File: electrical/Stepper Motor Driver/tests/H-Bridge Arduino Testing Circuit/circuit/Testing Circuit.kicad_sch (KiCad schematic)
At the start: 26 parts, among them M1 Stepper_Motor_bipolar, Q1 NMOS, Q2 NMOS, Q3 NMOS, Q4 NMOS, Q5 NMOS, Q6 NMOS, Q7 NMOS, Q8 NMOS, U1 UCC27710D, U2 UCC27710D, U3 UCC27710D, U4 UCC27710D

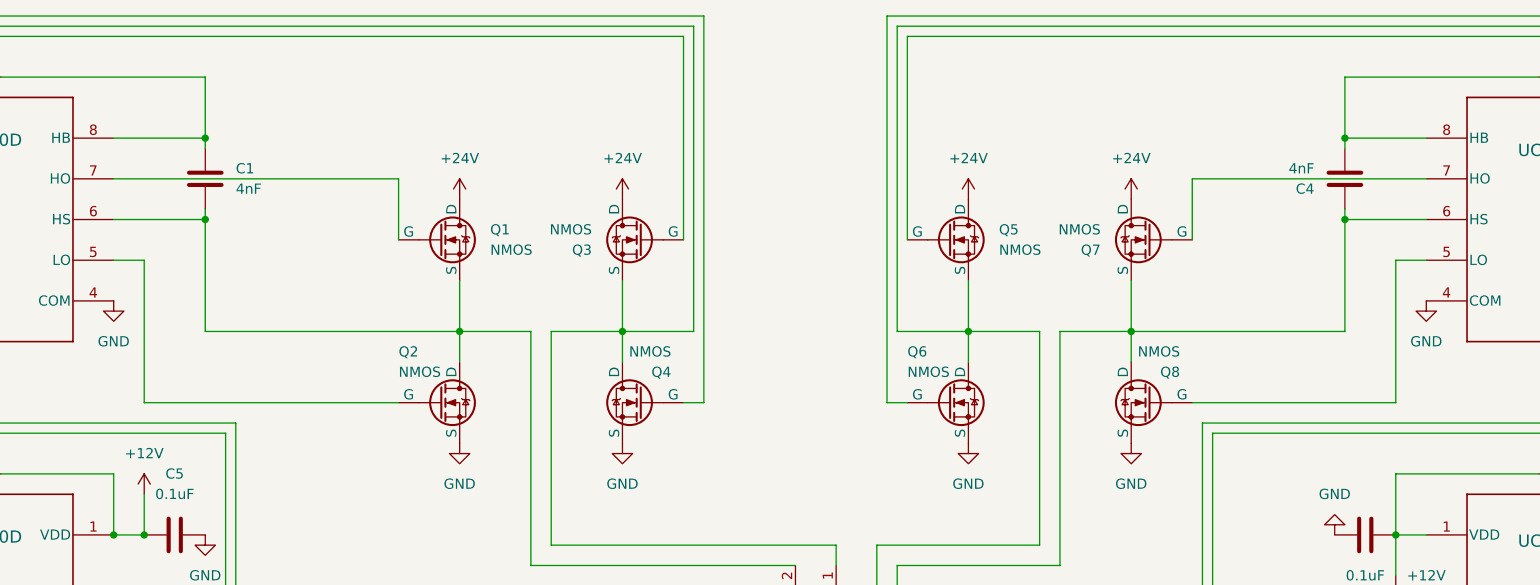
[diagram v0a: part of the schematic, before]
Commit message: Adding correct nMOS symbol
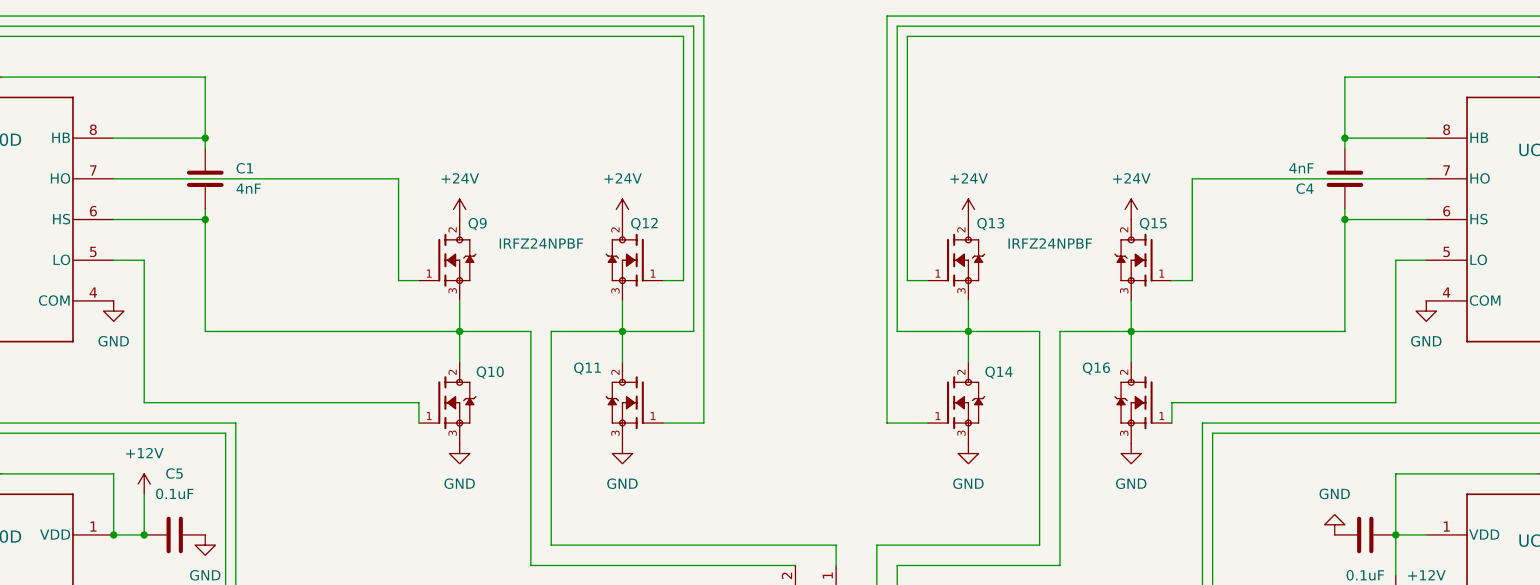
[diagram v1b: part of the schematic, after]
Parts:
- removed Q1, Q2, Q3, Q4, Q5, Q6, Q7, Q8: NMOS, symbol Simulation_SPICE:NMOS
- added Q10, Q11, Q12, Q13, Q14, Q15, Q16, Q9: IRFZ24NPBF, IRFZ24NPBF:TO254P1041X444X1930-3P, symbol IRFZ24NPBF:IRFZ24NPBF
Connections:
- net +24V: now also Q12.2, Q13.2, Q15.2, Q9.2
- net GND: now also Q10.3, Q11.3, Q14.3, Q16.3
- net at U1.5 (LO): now also Q10.1
- net at C1.2, M1.2 (-), U1.6 (HS): now also Q10.2, Q9.3
- net at U1.7 (HO): now also Q9.1
- net at U4.5 (LO): now also Q14.1
- net at C3.2, M1.3, U4.6 (HS): now also Q13.3, Q14.2
- net at U4.7 (HO): now also Q13.1
- net at U2.7 (HO): now also Q12.1
- net at C2.1, M1.1, U2.6 (HS): now also Q11.2, Q12.3
- net at U2.5 (LO): now also Q11.1
- net at U3.5 (LO): now also Q16.1
- net at C4.1, M1.4, U3.6 (HS): now also Q15.3, Q16.2
- net at U3.7 (HO): now also Q15.1

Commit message: Final MOSFET selection and spice models
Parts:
- removed Q10, Q11, Q12, Q13, Q14, Q15, Q16, Q9: IRFZ24NPBF, IRFZ24NPBF:TO254P1041X444X1930-3P, symbol IRFZ24NPBF:IRFZ24NPBF
- added Q1, Q2, Q3, Q4, Q5, Q6, Q7, Q8: IRF530NPBF, IRF530NPBF:TO254P1041X444X1930-3, symbol IRF530NPBF:IRF530NPBF
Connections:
- net +24V: now also Q1.2, Q4.2, Q5.2, Q7.2
- net GND: now also Q2.3, Q3.3, Q6.3, Q8.3
- net at U1.5 (LO): now also Q2.1
- net at C1.2, M1.2 (-), U1.6 (HS): now also Q1.3, Q2.2
- net at U1.7 (HO): now also Q1.1
- net at U4.5 (LO): now also Q6.1
- net at C3.2, M1.3, U4.6 (HS): now also Q5.3, Q6.2
- net at U4.7 (HO): now also Q5.1
- net at U3.5 (LO): now also Q8.1
- net at C4.1, M1.4, U3.6 (HS): now also Q7.3, Q8.2
- net at U2.7 (HO): now also Q4.1
- net at C2.1, M1.1, U2.6 (HS): now also Q3.2, Q4.3
- net at U3.7 (HO): now also Q7.1
- net at U2.5 (LO): now also Q3.1

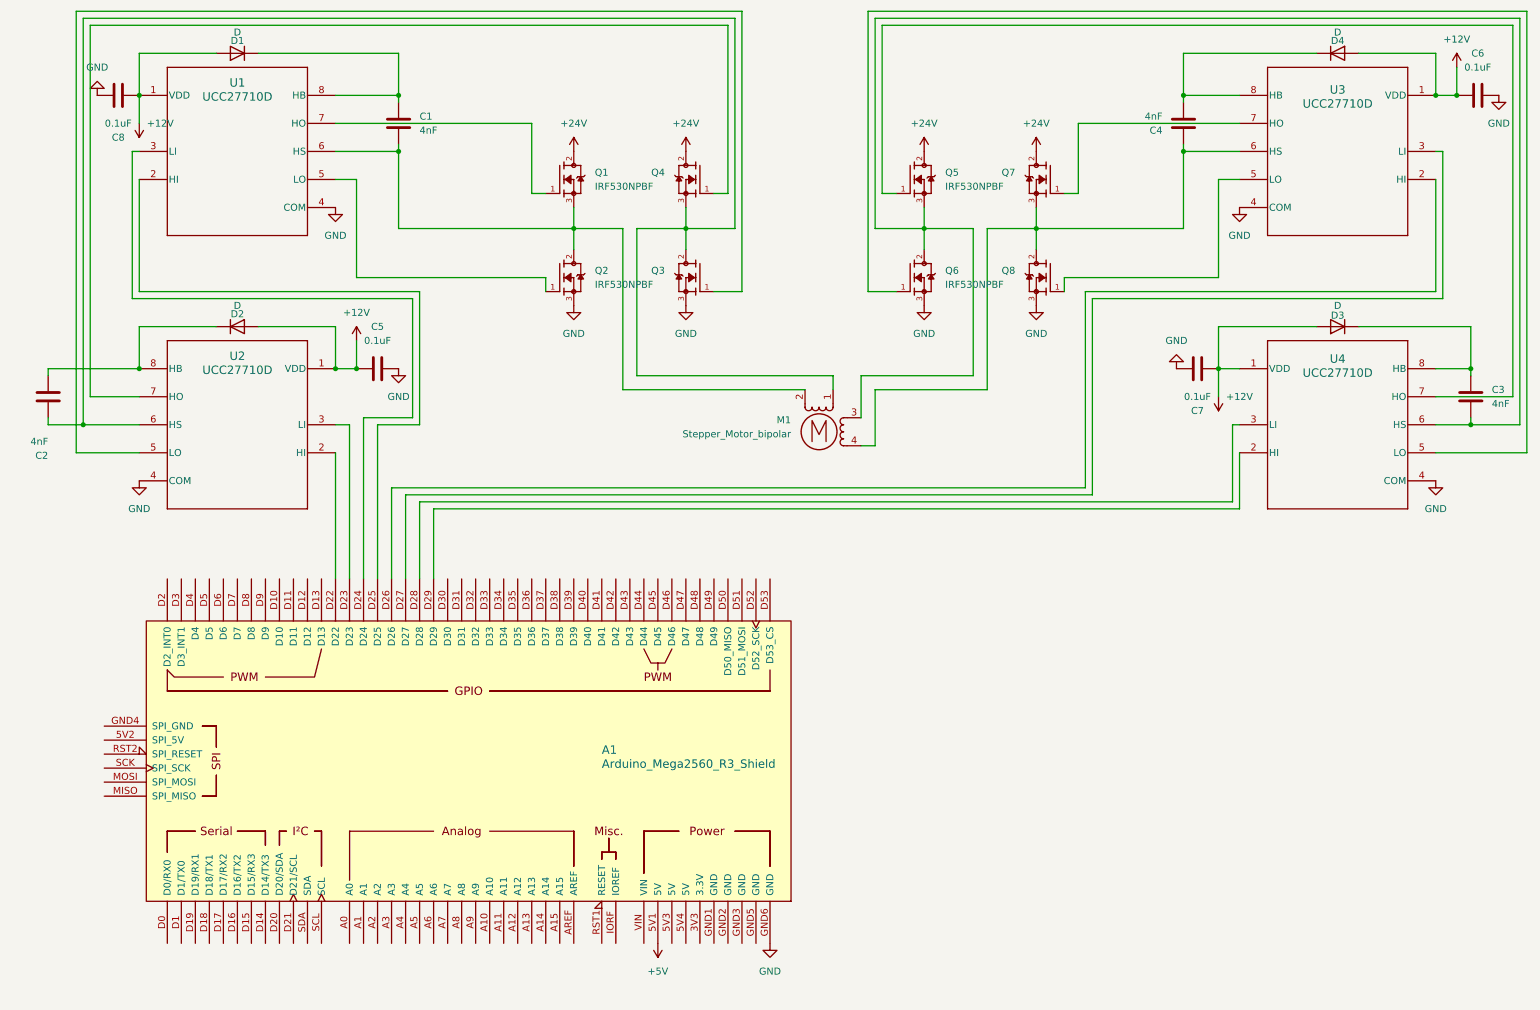
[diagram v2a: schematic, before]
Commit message: Adding motor spice model
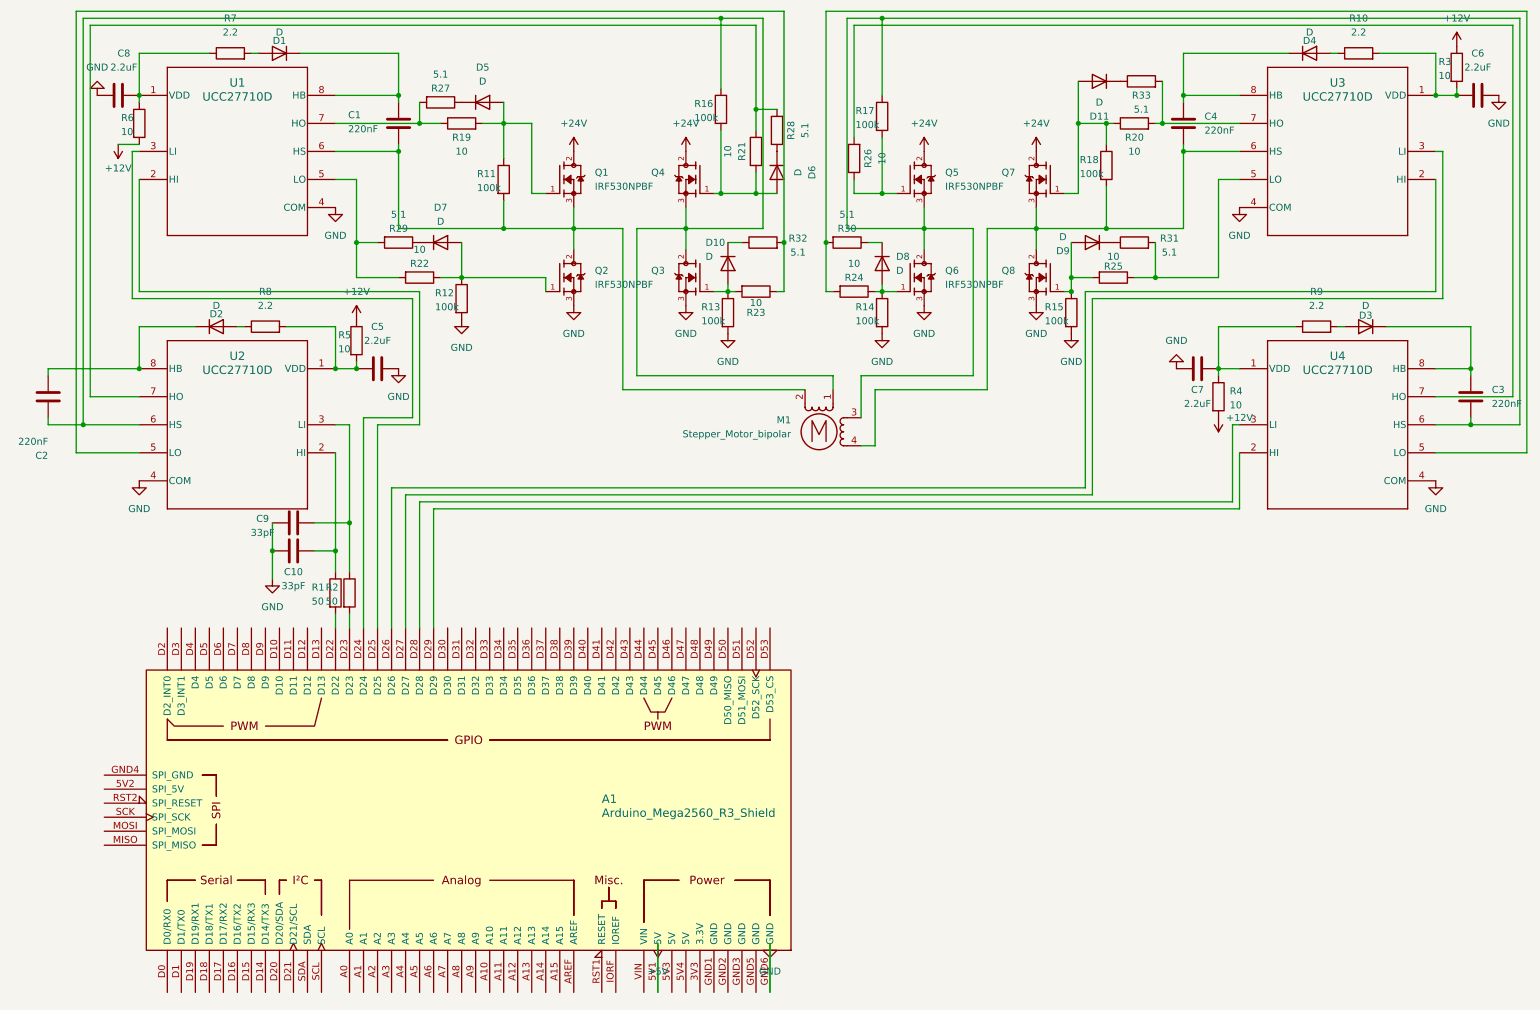
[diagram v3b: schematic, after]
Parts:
- added C10, C9: 33pF, symbol Device:C
- added D10, D11, D5, D6, D7, D8, D9: D, symbol Device:D
- added R1, R2: 50, symbol Device:R
- added R10, R7, R8, R9: 2.2, symbol Device:R
- added R11, R12, R13, R14, R15, R16, R17, R18: 100k, symbol Device:R
- added R19, R20, R21, R22, R23, R24, R25, R26, R3, R4, R5, R6: 10, symbol Device:R
- added R27, R28, R29, R30, R31, R32, R33: 5.1, symbol Device:R
- C1, C2, C3, C4: value 4nF -> 220nF
- C5, C6, C7, C8: value 0.1uF -> 2.2uF
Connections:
- net +12V: now also R3.1, R4.2, R5.1, R6.2; no longer C5.1, C6.1, C7.1, C8.1, D1.2 (A), D2.2 (A), D3.2 (A), D4.2 (A), U1.1 (VDD), U2.1 (VDD), U3.1 (VDD), U4.1 (VDD)
- net GND: now also C10.1, C9.1, R12.2, R13.2, R14.2, R15.2
- net at U1.5 (LO): now also R22.2, R29.2; no longer Q2.1
- net at C1.2, M1.2 (-), Q1.3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: now also R11.2
- net at U1.7 (HO): now also R19.1, R27.2; no longer Q1.1
- net at Q6.1: now also D8.2 (A), R14.1, R24.1; no longer U4.5 (LO)
- net at C3.2, M1.3, Q5.3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: now also R17.1
- net at Q5.1: now also R17.2, R26.1; no longer U4.7 (HO)
- net at U2.2 (HI): now also C10.2, R1.1; no longer A1.D22
- net at U2.3 (LI): now also C9.2, R2.1; no longer A1.D23
- net at U2.5 (LO): now also R23.1, R32.2; no longer Q3.1
- net at C2.1, M1.1, Q3.2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: now also R16.1
- net at U2.7 (HO): now also R21.1, R28.2; no longer Q4.1
- net at U3.5 (LO): now also R25.1, R31.2; no longer Q8.1
- net at C4.1, M1.4, Q7.3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: now also R18.2
- net at U3.7 (HO): now also R20.2, R33.2; no longer Q7.1
- new net: C8.1, R6.1, R7.1, U1.1 (VDD)
- new net: D10.2 (A), Q3.1, R13.1, R23.2
- new net: C7.1, R4.1, R9.1, U4.1 (VDD)
- new net: D6.1 (K), R28.1
- new net: D9.2 (A), Q8.1, R15.1, R25.2
- new net: D2.2 (A), R8.1
- new net: D6.2 (A), Q4.1, R16.2, R21.2
- new net: C5.1, R5.2, R8.2, U2.1 (VDD)
- new net: D4.2 (A), R10.1
- new net: C6.1, R10.2, R3.2, U3.1 (VDD)
- new net: D7.1 (K), R29.1
- new net: D7.2 (A), Q2.1, R12.1, R22.1
- new net: D9.1 (K), R31.1
- new net: D5.1 (K), R27.1
- new net: D1.2 (A), R7.2
- new net: R26.2, U4.7 (HO)
- new net: A1.D23, R2.2
- new net: D10.1 (K), R32.1
- new net: D11.1 (K), R33.1
- new net: D11.2 (A), Q7.1, R18.1, R20.1
- new net: D8.1 (K), R30.1
- new net: D5.2 (A), Q1.1, R11.1, R19.2
- new net: R24.2, R30.2, U4.5 (LO)
- new net: A1.D22, R1.2
- new net: D3.2 (A), R9.2
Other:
- moved on the sheet: A1, D1, D2, D3, D4

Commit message: Selecting diodes and adding all recommended components
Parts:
- removed D1, D10, D11, D2, D3, D4, D5, D6, D7, D8, D9: D, symbol Device:D
- added D1, D2, D3, D4: 1N5819, Diode_THT:D_DO-41_SOD81_P10.16mm_Horizontal, symbol Diode:1N5819
- added D13, D14, D15, D16, D17, D18, D19, D20: BAT43, Diode_THT:D_DO-35_SOD27_P7.62mm_Horizontal, symbol Diode:BAT43
- added R34: 5.1, symbol Device:R
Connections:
- net at C1.1, U1.8 (HB): now also D1.1 (K)
- net at Q3.1, R13.1, R23.2: now also D16.2 (A)
- net at R28.1: now also D15.1 (K)
- net at Q8.1, R15.1, R25.2: now also D18.2 (A)
- net at C2.2, U2.8 (HB): now also D2.1 (K)
- net at R8.1: now also D2.2 (A)
- net at Q4.1, R16.2, R21.2: now also D15.2 (A)
- net at Q6.1, R14.1, R24.1: now also D17.2 (A)
- net at Q5.1, R17.2, R26.1: now also D20.2 (A)
- net at R10.1: now also D4.2 (A)
- net at R29.1: now also D13.1 (K)
- net at Q2.1, R12.1, R22.1: now also D13.2 (A)
- net at R31.1: now also D18.1 (K)
- net at C4.2, U3.8 (HB): now also D4.1 (K)
- net at R27.1: now also D14.1 (K)
- net at R7.2: now also D1.2 (A)
- net at R26.2, U4.7 (HO): now also R34.2
- net at R32.1: now also D16.1 (K)
- net at R33.1: now also D19.1 (K)
- net at Q7.1, R18.1, R20.1: now also D19.2 (A)
- net at R30.1: now also D17.1 (K)
- net at Q1.1, R11.1, R19.2: now also D14.2 (A)
- net at C3.1, U4.8 (HB): now also D3.1 (K)
- net at R9.2: now also D3.2 (A)
- new net: D20.1 (K), R34.1

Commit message: Docs for H-Bridge + driver
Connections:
- net GND: no longer A1.GND6 (GND)
- net at C9.2, R2.1, U2.3 (LI): now also A1.D23
- net at R2.2: no longer A1.D23
- net at C10.2, R1.1, U2.2 (HI): now also A1.D22
- net at R1.2: no longer A1.D22
- net +5V: no longer names the net of A1.5V1 (5V)
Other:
- moved on the sheet: A1
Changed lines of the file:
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@@
 	)
 	(junction
+		(at 69.85 120.65)
+		(diameter 0)
+		(color 0 0 0 0)
+	)
+	(junction
 		(at 82.55 39.37)
 		(diameter 0)
@@
 	)
 	(junction
+		(at 67.31 120.65)
+		(diameter 0)
+		(color 0 0 0 0)
+	)
+	(junction
 		(at 67.31 116.84)
 		(diameter 0)
@@
 	(wire
 		(pts
-			(xy 125.73 196.85) (xy 125.73 187.96)
-		)
-		(stroke
-			(width 0)
-			(type default)
-		)
-	)
-	(wire
-		(pts
 			(xy 137.16 52.07) (xy 135.89 52.07)
 		)
@@
 	(wire
 		(pts
-			(xy 77.47 130.81) (xy 77.47 105.41)
+			(xy 77.47 132.08) (xy 77.47 105.41)
 		)
 		(stroke
@@
 	(wire
 		(pts
-			(xy 80.01 130.81) (xy 80.01 106.68)
+			(xy 80.01 132.08) (xy 80.01 106.68)
 		)
 		(stroke
@@
 	(wire
 		(pts
-			(xy 67.31 128.27) (xy 67.31 130.81)
+			(xy 67.31 120.65) (xy 67.31 132.08)
 		)
 		(stroke
@@
 	(wire
 		(pts
-			(xy 69.85 128.27) (xy 69.85 130.81)
-		)
-		(stroke
-			(width 0)
-			(type default)
-		)
-	)
-	(wire
-		(pts
 			(xy 80.01 106.68) (xy 204.47 106.68)
 		)
@@
 	(wire
 		(pts
-			(xy 74.93 93.98) (xy 74.93 130.81)
+			(xy 74.93 93.98) (xy 74.93 132.08)
 		)
 		(stroke
@@
 	(wire
 		(pts
-			(xy 146.05 196.85) (xy 146.05 187.96)
-		)
-		(stroke
-			(width 0)
-			(type default)
-		)
-	)
-	(wire
-		(pts
 			(xy 207.01 58.42) (xy 194.31 58.42)
 		)
@@
 	(wire
 		(pts
+			(xy 69.85 120.65) (xy 69.85 132.08)
+		)
+		(stroke
+			(width 0)
+			(type default)
+		)
+	)
+	(wire
+		(pts
 			(xy 71.12 67.31) (xy 78.74 67.31)
 		)
@@
 	(wire
 		(pts
-			(xy 85.09 130.81) (xy 85.09 109.22)
+			(xy 85.09 132.08) (xy 85.09 109.22)
 		)
 		(stroke
@@
 	(wire
 		(pts
-			(xy 72.39 130.81) (xy 72.39 92.71)
+			(xy 72.39 132.08) (xy 72.39 92.71)
 		)
 		(stroke
@@
 	(wire
 		(pts
-			(xy 82.55 130.81) (xy 82.55 107.95)
+			(xy 82.55 132.08) (xy 82.55 107.95)
 		)
 		(stroke
@@
 	)
 	(symbol
-		(lib_id "power:+5V")
-		(at 125.73 187.96 180)
-		(unit 1)
-		(body_style 1)
-		(exclude_from_sim no)
-		(in_bom yes)
-		(on_board yes)
-		(in_pos_files yes)
-		(dnp no)
-		(fields_autoplaced yes)
-		(property "Reference" "#PWR021"
-			(at 125.73 184.15 0)
-			(hide yes)
-			(show_name no)
-			(do_not_autoplace no)
-			(effects
-				(font
-					(size 1.27 1.27)
-				)
-			)
-		)
-		(property "Value" "+5V"
-			(at 125.73 193.04 0)
-			(show_name no)
-			(do_not_autoplace no)
-			(effects
-				(font
-					(size 1.27 1.27)
-				)
-			)
-		)
-		(property "Footprint" ""
-			(at 125.73 187.96 0)
-			(hide yes)
-			(show_name no)
-			(do_not_autoplace no)
-			(effects
-				(font
-					(size 1.27 1.27)
-				)
-			)
-		)
-		(property "Datasheet" ""
-			(at 125.73 187.96 0)
-			(hide yes)
-			(show_name no)
-			(do_not_autoplace no)
-			(effects
-				(font
-					(size 1.27 1.27)
-				)
-			)
-		)
-		(property "Description" "Power symbol creates a global label with name \"+5V\""
-			(at 125.73 187.96 0)
-			(hide yes)
-			(show_name no)
-			(do_not_autoplace no)
-			(effects
-				(font
-					(size 1.27 1.27)
-				)
-			)
-		)
-		(pin "1"
-		)
-		(instances
-			(project "Testing Circuit"
-				(path "/c25060f1-f2f3-4cbd-b6ee-5f66e19502f5"
-					(reference "#PWR021")
-					(unit 1)
-				)
-			)
-		)
-	)
-	(symbol
-		(lib_id "power:GND")
-		(at 146.05 187.96 0)
-		(unit 1)
-		(body_style 1)
-		(exclude_from_sim no)
-		(in_bom yes)
-		(on_board yes)
-		(in_pos_files yes)
-		(dnp no)
-		(fields_autoplaced yes)
-		(property "Reference" "#PWR022"
-			(at 146.05 194.31 0)
-			(hide yes)
-			(show_name no)
-			(do_not_autoplace no)
-			(effects
-				(font
-					(size 1.27 1.27)
-				)
-			)
-		)
-		(property "Value" "GND"
-			(at 146.05 193.04 0)
-			(show_name no)
-			(do_not_autoplace no)
-			(effects
-				(font
-					(size 1.27 1.27)
-				)
-			)
-		)
-		(property "Footprint" ""
-			(at 146.05 187.96 0)
-			(hide yes)
-			(show_name no)
-			(do_not_autoplace no)
-			(effects
-				(font
-					(size 1.27 1.27)
-				)
-			)
-		)
-		(property "Datasheet" ""
-			(at 146.05 187.96 0)
-			(hide yes)
-			(show_name no)
-			(do_not_autoplace no)
-			(effects
-				(font
-					(size 1.27 1.27)
-				)
-			)
-		)
-		(property "Description" "Power symbol creates a global label with name \"GND\" , ground"
-			(at 146.05 187.96 0)
-			(hide yes)
-			(show_name no)
-			(do_not_autoplace no)
-			(effects
-				(font
-					(size 1.27 1.27)
-				)
-			)
-		)
-		(pin "1"
-		)
-		(instances
-			(project "Testing Circuit"
-				(path "/c25060f1-f2f3-4cbd-b6ee-5f66e19502f5"
-					(reference "#PWR022")
-					(unit 1)
-				)
-			)
-		)
-	)
-	(symbol
 		(lib_id "Device:C")
 		(at 223.52 83.82 270)
@@
 	(symbol
 		(lib_id "arduino-library:Arduino_Mega2560_R3_Shield")
-		(at 91.44 163.83 90)
+		(at 91.44 165.1 90)
 		(unit 1)
 		(body_style 1)
@@
 		(dnp no)
 		(property "Reference" "A1"
-			(at 115.57 161.798 90)
+			(at 115.57 163.068 90)
 			(show_name no)
 			(do_not_autoplace no)
@@
 		)
 		(property "Value" "Arduino_Mega2560_R3_Shield"
-			(at 115.57 164.338 90)
+			(at 115.57 165.608 90)
 			(show_name no)
 			(do_not_autoplace no)
@@
 		)
 		(property "Footprint" "PCM_arduino-library:Arduino_Mega2560_R3_Shield"
-			(at 165.1 163.83 0)
+			(at 165.1 165.1 0)
 			(hide yes)
 			(show_name no)
@@
 		)
 		(property "Datasheet" "https://docs.arduino.cc/hardware/mega-2560"
-			(at 161.29 163.83 0)
+			(at 161.29 165.1 0)
 			(hide yes)
 			(show_name no)
@@
 		)
 		(property "Description" "Shield for Arduino Mega 2560 R3"
-			(at 91.44 163.83 0)
+			(at 91.44 165.1 0)
 			(hide yes)
 			(show_name no)
